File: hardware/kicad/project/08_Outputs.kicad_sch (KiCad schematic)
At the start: 0 parts

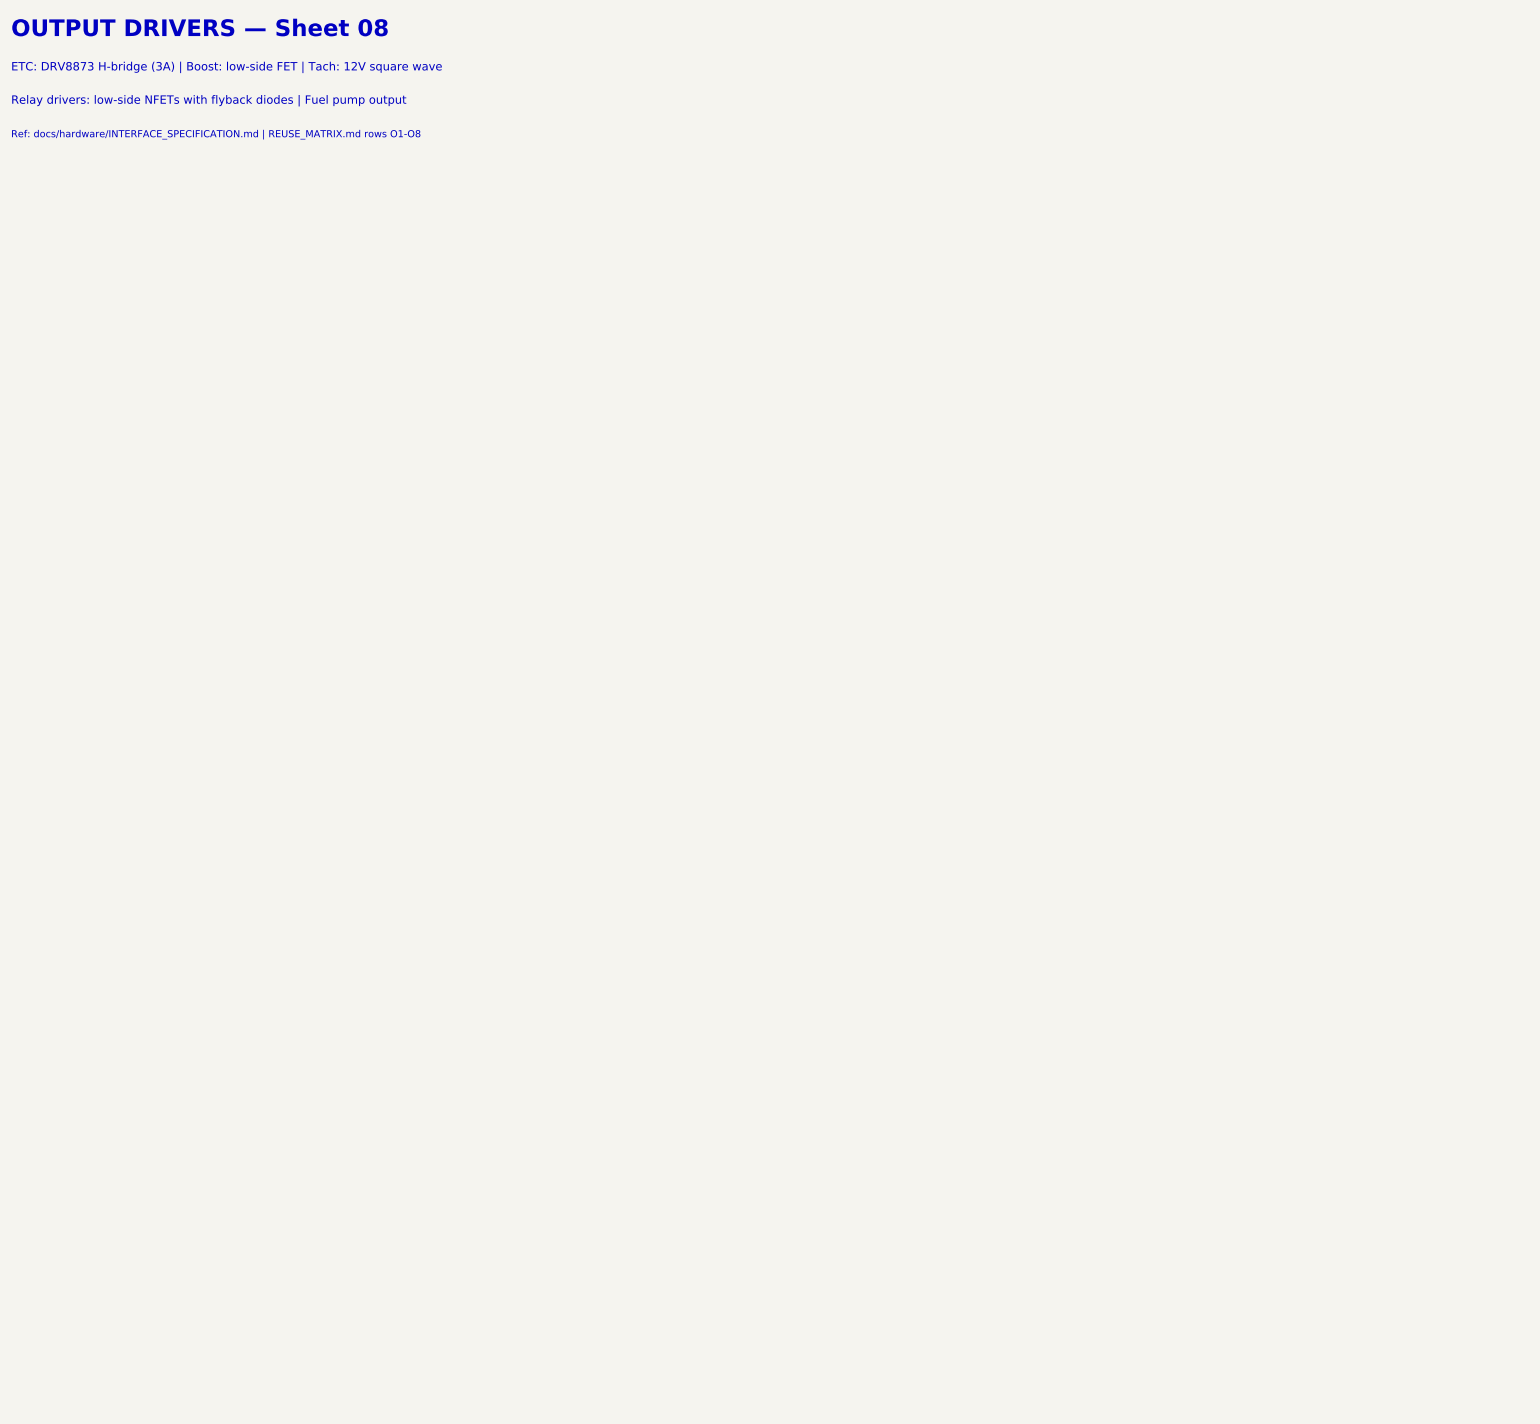
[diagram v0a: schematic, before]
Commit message: feat(hardware): TB-HW-002 — populate all 12 schematic sheets with components
Populated 235 component symbols across all 12 KiCad schematic sheets:
- 01_Power: Reverse polarity, TVS (SMCJ33A), buck (LMR33630), LDO (TPS7A1633), VREF (REF5050) — 30 symbols
- 02_MCU: S32K344 (6 units), clock (40MHz+32kHz), decoupling, reset, boot config, LEDs — 30 symbols
- 03_CAN: 4x TJA1043 with CM chokes (ACT45B-510), split termination, bus filter caps — 36 symbols
- 04_USB: Molex USB-C, TPD2EUSB30 ESD, CC resistors, eFuse, Ethernet PHY footprint — 9 symbols
- 05_Inputs: 8 analog channels (RC+clamp), 2x CJ125 WBO2, 2x TLE2072 knock amps — 50 symbols
- 06_Injectors: TLE8888-2QK (8-ch P&H), flyback diodes, current sense — 14 symbols
- 07_Ignition: 6x ISL9V3040S3 IGBTs with gate resistors (100R), pull-downs (10k) — 24 symbols
- 08_Outputs: DRV8873 ETC H-bridge, TLE8110ED low-side (boost+relays), BTS4140N tach — 12 symbols
- 09_Protection: TPS3850G33 watchdog, safe-state FET, ESD diodes (PESD5V0) — 14 symbols
- 10_Connectors: 42-pin Deutsch DTM (2 units), 2x CAN 4-pin, diagnostic 4-pin — 5 symbols
- 11_Programming: TC2050 SWD, 8 test points, production security notes — 11 symbols
- 00_Cover: Block diagram, BOM summary, spec references, revision history

Symbol library: 18 custom symbols with complete pin assignments
Components from COMPONENT_SELECTION.md r0.1
42-pin connector per INTERFACE_SPECIFICATION.md (authority)
All MCU pins per MCU_SELECTION.md pin allocation
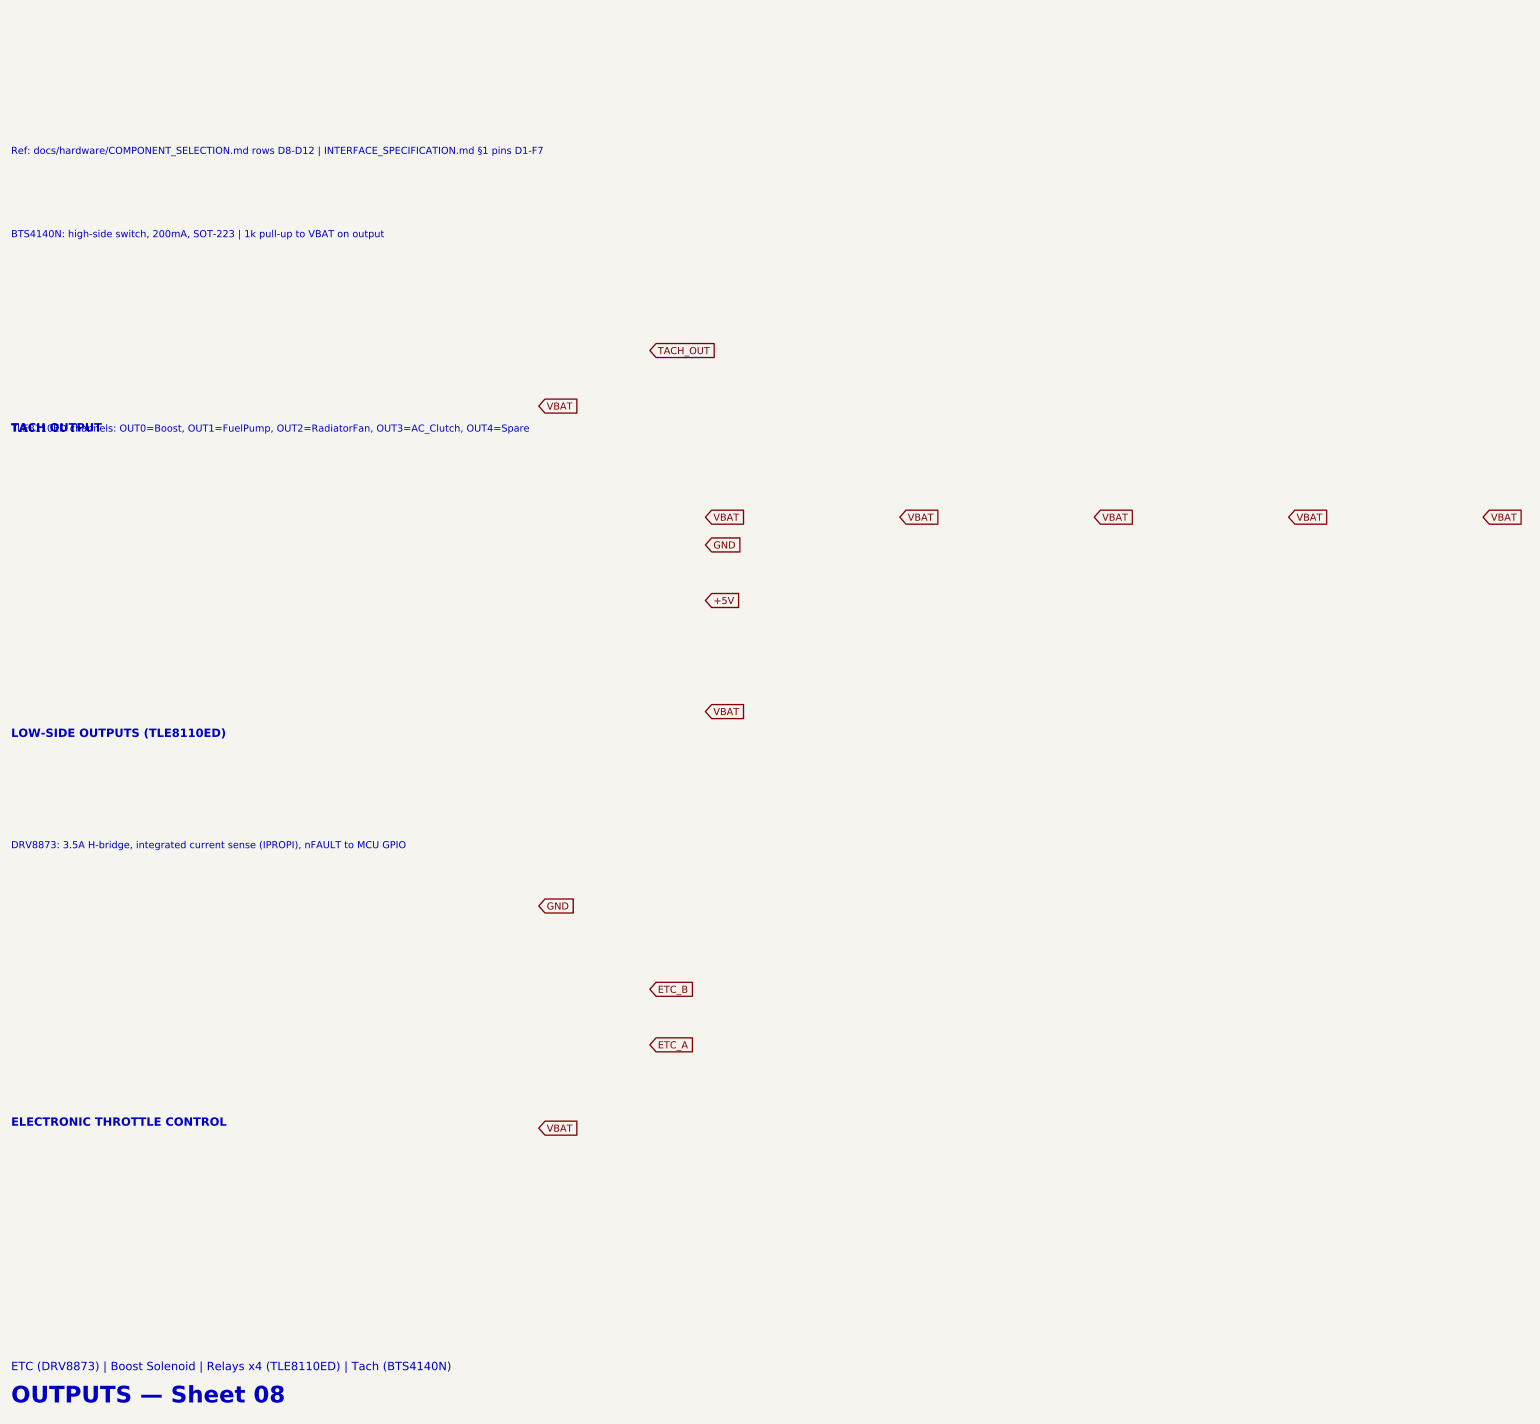
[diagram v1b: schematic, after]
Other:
- note added: "BTS4140N: high-side switch, 200mA, SOT-223 | 1k pull-up to VBAT on output"
- note added: "DRV8873: 3.5A H-bridge, integrated current sense (IPROPI), nFAULT to MCU GPIO"
- note added: "ELECTRONIC THROTTLE CONTROL"
- note added: "ETC (DRV8873) | Boost Solenoid | Relays x4 (TLE8110ED) | Tach (BTS4140N)"
- note added: "LOW-SIDE OUTPUTS (TLE8110ED)"
- note added: "OUTPUTS — Sheet 08"
- note added: "Ref: docs/hardware/COMPONENT_SELECTION.md rows D8-D12 | INTERFACE_SPECIFICATION.md §1 pins D1-F7"
- note added: "TACH OUTPUT"
- note added: "TLE8110ED channels: OUT0=Boost, OUT1=FuelPump, OUT2=RadiatorFan, OUT3=AC_Clutch, OUT4=Spare"
- note removed: "ETC: DRV8873 H-bridge (3A) | Boost: low-side FET | Tach: 12V square wave"
- note removed: "OUTPUT DRIVERS — Sheet 08"
- note removed: "Ref: docs/hardware/INTERFACE_SPECIFICATION.md | REUSE_MATRIX.md rows O1-O8"
- note removed: "Relay drivers: low-side NFETs with flyback diodes | Fuel pump output"
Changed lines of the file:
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@@
-(kicad_sch (version 20240108) (generator "eeschema")
+(kicad_sch (version 20240108) (generator "7100CPT-schematic-gen")
   (paper "A3")
   (title_block
     (title "7100CPT ECU — ETC, Boost, Relays, Tach")
     (date "2026-07-03")
-    (rev "0.1")
+    (rev "0.2")
     (company "${COMPANY}")
-    (comment 1 "ETC (DRV8873), boost solenoid, relays (low-side), tachometer")
+    (comment 1 "ETC (DRV8873), boost solenoid, relays (TLE8110ED), tach (BTS4140N)")
     (comment 2 "NXP S32K344 | rusEFI Firmware | IPC Class 3")
     (comment 3 "High-Tg FR-4 (TG170+) | ENIG | 1.6 mm")
-    (comment 4 "REUSE_MATRIX.md — NXP Reference Following")
+    (comment 4 "Phase 0 Approved | REUSE_MATRIX gate passed")
     (comment 5 "-40C to +85C | IP67 Target | 6-Layer")
   )
-  (symbol_instances)
-  (text "OUTPUT DRIVERS — Sheet 08"
-    (at 25 24 0) (effects (font (size 3.0 3.0) bold) (justify left bottom)))
-  (text "ETC: DRV8873 H-bridge (3A) | Boost: low-side FET | Tach: 12V square wave"
-    (at 25 30 0) (effects (font (size 1.5 1.5)) (justify left bottom)))
-  (text "Relay drivers: low-side NFETs with flyback diodes | Fuel pump output"
-    (at 25 36 0) (effects (font (size 1.5 1.5)) (justify left bottom)))
-  (text "Ref: docs/hardware/INTERFACE_SPECIFICATION.md | REUSE_MATRIX.md rows O1-O8"
-    (at 25 42 0) (effects (font (size 1.27 1.27)) (justify left bottom)))
+  (symbol_instances
+  (symbol (lib_id "7100CPT:DRV8873") (at 120 200 0) (unit 1)
+    (exclude_from_sim yes) (in_bom yes) (on_board yes) (dnp no)
+    (property "Reference" "U42" (at 120 200 0) (effects (font (size 1.27 1.27))))
+    (property "Value" "DRV8873HPWPR" (at 120 193.65 0) (effects (font (size 1.27 1.27))))
+  )
+  (symbol (lib_id "Device:CP") (at 120 220 0) (unit 1)
+    (exclude_from_sim yes) (in_bom yes) (on_board yes) (dnp no)
+    (property "Reference" "C110" (at 120 220 0) (effects (font (size 1.27 1.27))))
+    (property "Value" "100uF_35V_Elec" (at 120 213.65 0) (effects (font (size 1.27 1.27))))
+  )
+  (symbol (lib_id "Device:R") (at 150 185 0) (unit 1)
+    (exclude_from_sim yes) (in_bom yes) (on_board yes) (dnp no)
+    (property "Reference" "R100" (at 150 185 0) (effects (font (size 1.27 1.27))))
+    (property "Value" "1k" (at 150 178.65 0) (effects (font (size 1.27 1.27))))
+  )
+  (symbol (lib_id "Device:C") (at 150 175 0) (unit 1)
+    (exclude_from_sim yes) (in_bom yes) (on_board yes) (dnp no)
+    (property "Reference" "C111" (at 150 175 0) (effects (font (size 1.27 1.27))))
+    (property "Value" "10nF_50V_X7R" (at 150 168.65 0) (effects (font (size 1.27 1.27))))
+  )
+  (symbol (lib_id "7100CPT:TLE8110ED") (at 150 130 0) (unit 1)
+    (exclude_from_sim yes) (in_bom yes) (on_board yes) (dnp no)
+    (property "Reference" "U43" (at 150 130 0) (effects (font (size 1.27 1.27))))
+    (property "Value" "TLE8110ED" (at 150 123.65 0) (effects (font (size 1.27 1.27))))
+  )
+  (symbol (lib_id "Device:D_Schottky") (at 150 105 0) (unit 1)
+    (exclude_from_sim yes) (in_bom yes) (on_board yes) (dnp no)
+    (property "Reference" "D50" (at 150 105 0) (effects (font (size 1.27 1.27))))
+    (property "Value" "SS34" (at 150 98.65 0) (effects (font (size 1.27 1.27))))
+  )
+  (symbol (lib_id "Device:D_Schottky") (at 185 105 0) (unit 1)
+    (exclude_from_sim yes) (in_bom yes) (on_board yes) (dnp no)
+    (property "Reference" "D51" (at 185 105 0) (effects (font (size 1.27 1.27))))
+    (property "Value" "SS34" (at 185 98.65 0) (effects (font (size 1.27 1.27))))
+  )
+  (symbol (lib_id "Device:D_Schottky") (at 220 105 0) (unit 1)
+    (exclude_from_sim yes) (in_bom yes) (on_board yes) (dnp no)
+    (property "Reference" "D52" (at 220 105 0) (effects (font (size 1.27 1.27))))
+    (property "Value" "SS34" (at 220 98.65 0) (effects (font (size 1.27 1.27))))
+  )
+  (symbol (lib_id "Device:D_Schottky") (at 255 105 0) (unit 1)
+    (exclude_from_sim yes) (in_bom yes) (on_board yes) (dnp no)
+    (property "Reference" "D53" (at 255 105 0) (effects (font (size 1.27 1.27))))
+    (property "Value" "SS34" (at 255 98.65 0) (effects (font (size 1.27 1.27))))
+  )
+  (symbol (lib_id "Device:D_Schottky") (at 290 105 0) (unit 1)
+    (exclude_from_sim yes) (in_bom yes) (on_board yes) (dnp no)
+    (property "Reference" "D54" (at 290 105 0) (effects (font (size 1.27 1.27))))
+    (property "Value" "SS34" (at 290 98.65 0) (effects (font (size 1.27 1.27))))
+  )
+  (symbol (lib_id "7100CPT:BTS4140N") (at 120 80 0) (unit 1)
+    (exclude_from_sim yes) (in_bom yes) (on_board yes) (dnp no)
+    (property "Reference" "U44" (at 120 80 0) (effects (font (size 1.27 1.27))))
+    (property "Value" "BTS4140N" (at 120 73.65 0) (effects (font (size 1.27 1.27))))
+  )
+  (symbol (lib_id "Device:R") (at 90 80 0) (unit 1)
+    (exclude_from_sim yes) (in_bom yes) (on_board yes) (dnp no)
+    (property "Reference" "R105" (at 90 80 0) (effects (font (size 1.27 1.27))))
+    (property "Value" "1k" (at 90 73.65 0) (effects (font (size 1.27 1.27))))
+  )
+  )
+  (text "OUTPUTS — Sheet 08" (at 25 270 0) (effects (font (size 3.0 3.0) bold) (justify left bottom)))
+  (text "ETC (DRV8873) | Boost Solenoid | Relays x4 (TLE8110ED) | Tach (BTS4140N)" (at 25 264 0) (effects (font (size 1.5 1.5)) (justify left bottom)))
+  (text "ELECTRONIC THROTTLE CONTROL" (at 25 220 0) (effects (font (size 1.5 1.5) bold) (justify left bottom)))
+  (text "DRV8873: 3.5A H-bridge, integrated current sense (IPROPI), nFAULT to MCU GPIO" (at 25 170 0) (effects (font (size 1.27 1.27)) (justify left bottom)))
+  (text "LOW-SIDE OUTPUTS (TLE8110ED)" (at 25 150 0) (effects (font (size 1.5 1.5) bold) (justify left bottom)))
+  (text "TLE8110ED channels: OUT0=Boost, OUT1=FuelPump, OUT2=RadiatorFan, OUT3=AC_Clutch, OUT4=Spare" (at 25 95 0) (effects (font (size 1.27 1.27)) (justify left bottom)))
+  (text "TACH OUTPUT" (at 25 95 0) (effects (font (size 1.5 1.5) bold) (justify left bottom)))
+  (text "BTS4140N: high-side switch, 200mA, SOT-223 | 1k pull-up to VBAT on output" (at 25 60 0) (effects (font (size 1.27 1.27)) (justify left bottom)))
+  (text "Ref: docs/hardware/COMPONENT_SELECTION.md rows D8-D12 | INTERFACE_SPECIFICATION.md §1 pins D1-F7" (at 25 45 0) (effects (font (size 1.27 1.27)) (justify left bottom)))
+  (global_label "VBAT" (shape input) (at 120 220 0) (effects (font (size 1.27 1.27))))
+  (global_label "GND" (shape input) (at 120 180 0) (effects (font (size 1.27 1.27))))
+  (global_label "ETC_A" (shape input) (at 140 205 0) (effects (font (size 1.27 1.27))))
+  (global_label "ETC_B" (shape input) (at 140 195 0) (effects (font (size 1.27 1.27))))
+  (global_label "VBAT" (shape input) (at 150 110 0) (effects (font (size 1.27 1.27))))
+  (global_label "VBAT" (shape input) (at 185 110 0) (effects (font (size 1.27 1.27))))
+  (global_label "VBAT" (shape input) (at 220 110 0) (effects (font (size 1.27 1.27))))
+  (global_label "VBAT" (shape input) (at 255 110 0) (effects (font (size 1.27 1.27))))
+  (global_label "VBAT" (shape input) (at 290 110 0) (effects (font (size 1.27 1.27))))
+  (global_label "VBAT" (shape input) (at 150 145 0) (effects (font (size 1.27 1.27))))
+  (global_label "+5V" (shape input) (at 150 125 0) (effects (font (size 1.27 1.27))))
+  (global_label "GND" (shape input) (at 150 115 0) (effects (font (size 1.27 1.27))))
+  (global_label "VBAT" (shape input) (at 120 90 0) (effects (font (size 1.27 1.27))))
+  (global_label "TACH_OUT" (shape input) (at 140 80 0) (effects (font (size 1.27 1.27))))
   (sheet_instances
     (path "/08_outputs/" (page "9"))
